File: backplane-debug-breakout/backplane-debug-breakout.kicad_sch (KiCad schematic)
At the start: 8 parts, among them J1 Conn_02x08_Odd_Even, J2 Conn_01x04, J3 Conn_01x01_Socket, J4 Conn_01x01_Socket, J5 Conn_01x04, SW1 SW_Push

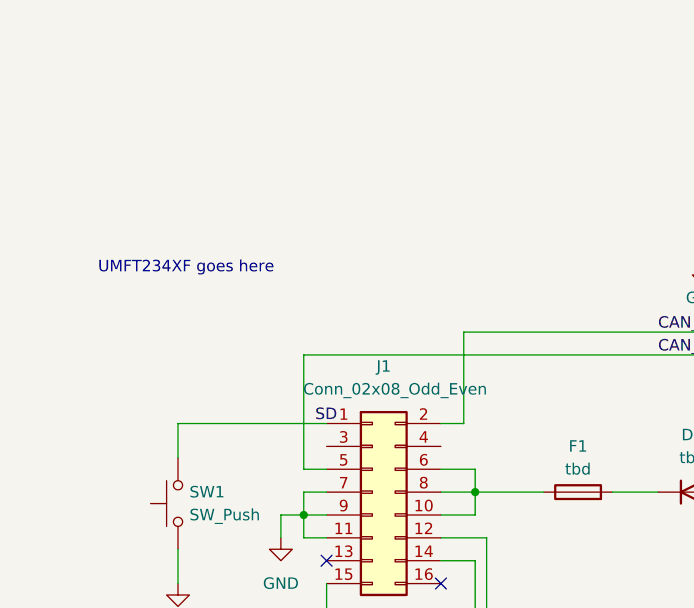
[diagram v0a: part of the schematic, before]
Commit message: added UMFT234XF to schematic
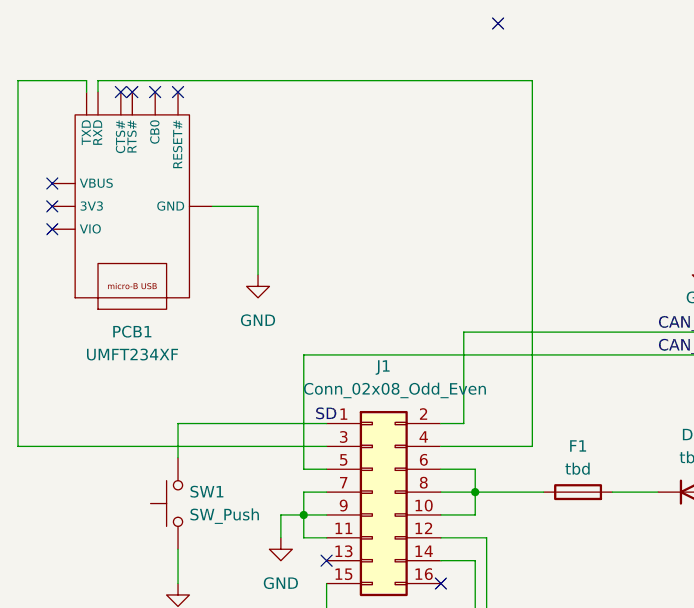
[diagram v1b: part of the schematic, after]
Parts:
- added PCB1: UMFT234XF, symbol oresat-pcbs:UMFT234XF
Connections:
- net GND: now also PCB1.P4 (GND)
- net at J1.3 (Pin_3): now also PCB1.P7 (TXD)
- net at J1.4 (Pin_4): now also PCB1.P9 (RXD)
- no-connect marks 3 -> 11
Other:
- note removed: "UMFT234XF goes here"
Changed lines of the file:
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@@
   (junction (at 120.65 80.01) (diameter 0) (color 0 0 0 0)
   )
+  (no_connect (at 123.19 27.94))
+  (no_connect (at 73.66 48.26))
   (no_connect (at 148.59 67.31))
+  (no_connect (at 81.28 35.56))
+  (no_connect (at 82.55 35.56))
+  (no_connect (at 73.66 50.8))
   (no_connect (at 104.14 87.63))
+  (no_connect (at 85.09 35.56))
+  (no_connect (at 73.66 45.72))
+  (no_connect (at 87.63 35.56))
   (no_connect (at 116.84 90.17))
   (wire (pts (xy 101.6 82.55) (xy 104.14 82.55))
@@
     (stroke (width 0) (type default))
   )
+  (wire (pts (xy 96.52 48.26) (xy 96.52 55.88))
+    (stroke (width 0) (type default))
+  )
   (wire (pts (xy 101.6 77.47) (xy 101.6 64.77))
     (stroke (width 0) (type default))
@@
     (stroke (width 0) (type default))
   )
+  (wire (pts (xy 69.85 74.93) (xy 104.14 74.93))
+    (stroke (width 0) (type default))
+  )
   (wire (pts (xy 148.59 59.69) (xy 148.59 53.34))
     (stroke (width 0) (type default))
   )
+  (wire (pts (xy 77.47 34.29) (xy 69.85 34.29))
+    (stroke (width 0) (type default))
+  )
   (wire (pts (xy 104.14 77.47) (xy 101.6 77.47))
     (stroke (width 0) (type default))
@@
     (stroke (width 0) (type default))
   )
+  (wire (pts (xy 127 34.29) (xy 127 74.93))
+    (stroke (width 0) (type default))
+  )
   (wire (pts (xy 104.14 80.01) (xy 101.6 80.01))
     (stroke (width 0) (type default))
@@
     (stroke (width 0) (type default))
   )
+  (wire (pts (xy 77.47 35.56) (xy 77.47 34.29))
+    (stroke (width 0) (type default))
+  )
   (wire (pts (xy 119.38 62.23) (xy 148.59 62.23))
     (stroke (width 0) (type default))
@@
     (stroke (width 0) (type default))
   )
+  (wire (pts (xy 78.74 34.29) (xy 127 34.29))
+    (stroke (width 0) (type default))
+  )
   (wire (pts (xy 148.59 80.01) (xy 154.94 80.01))
     (stroke (width 0) (type default))
@@
     (stroke (width 0) (type default))
   )
+  (wire (pts (xy 78.74 35.56) (xy 78.74 34.29))
+    (stroke (width 0) (type default))
+  )
+  (wire (pts (xy 69.85 34.29) (xy 69.85 74.93))
+    (stroke (width 0) (type default))
+  )
+  (wire (pts (xy 127 74.93) (xy 116.84 74.93))
+    (stroke (width 0) (type default))
+  )
   (wire (pts (xy 116.84 87.63) (xy 120.65 87.63))
     (stroke (width 0) (type default))
@@
     (stroke (width 0) (type default))
   )
+  (wire (pts (xy 91.44 48.26) (xy 96.52 48.26))
+    (stroke (width 0) (type default))
+  )
   (text "To vulCAN" (at 156.21 64.77 0)
     (effects (font (size 1.27 1.27)) (justify left bottom))
   )
-  (text "UMFT234XF goes here\n" (at 78.74 55.88 0)
-    (effects (font (size 1.27 1.27)) (justify left bottom))
-  )
   (text "OPD" (at 154.94 100.33 0)
     (effects (font (size 1.27 1.27)) (justify left bottom))
@@
     (pin "1")
     (instances
-      (project "flatsat-backplane-breakout-debug"
+      (project "backplane-debug-breakout"
         (path "/3c6f9748-3b52-445b-9cee-a3f7ec926272"
           (reference "D1") (unit 1)
@@
     )
   )
+  (symbol (lib_id "power:GND") (at 96.52 55.88 0) (unit 1)
+    (in_bom yes) (on_board yes) (dnp no) (fields_autoplaced)
+    (property "Reference" "#PWR06" (at 96.52 62.23 0)
+      (effects (font (size 1.27 1.27)) hide)
+    )
+    (property "Value" "GND" (at 96.52 60.96 0)
+      (effects (font (size 1.27 1.27)))
+    )
+    (property "Footprint" "" (at 96.52 55.88 0)
+      (effects (font (size 1.27 1.27)) hide)
+    )
+    (property "Datasheet" "" (at 96.52 55.88 0)
+      (effects (font (size 1.27 1.27)) hide)
+    )
+    (pin "1")
+    (instances
+      (project "backplane-debug-breakout"
+        (path "/3c6f9748-3b52-445b-9cee-a3f7ec926272"
+          (reference "#PWR06") (unit 1)
+        )
+      )
+    )
+  )
   (symbol (lib_id "Connector:Conn_01x01_Socket") (at 160.02 83.82 0) (unit 1)
     (in_bom yes) (on_board yes) (dnp no) (fields_autoplaced)
@@
     (pin "1")
     (instances
-      (project "flatsat-backplane-breakout-debug"
+      (project "backplane-debug-breakout"
         (path "/3c6f9748-3b52-445b-9cee-a3f7ec926272"
           (reference "J4") (unit 1)
@@
     (pin "1")
     (instances
-      (project "flatsat-backplane-breakout-debug"
+      (project "backplane-debug-breakout"
         (path "/3c6f9748-3b52-445b-9cee-a3f7ec926272"
           (reference "#PWR01") (unit 1)
@@
     (pin "2")
     (instances
-      (project "flatsat-backplane-breakout-debug"
+      (project "backplane-debug-breakout"
         (path "/3c6f9748-3b52-445b-9cee-a3f7ec926272"
           (reference "J1") (unit 1)
@@
     (pin "3")
     (instances
-      (project "flatsat-backplane-breakout-debug"
+      (project "backplane-debug-breakout"
         (path "/3c6f9748-3b52-445b-9cee-a3f7ec926272"
           (reference "J5") (unit 1)
@@
     (pin "2")
     (instances
-      (project "flatsat-backplane-breakout-debug"
+      (project "backplane-debug-breakout"
         (path "/3c6f9748-3b52-445b-9cee-a3f7ec926272"
           (reference "SW1") (unit 1)
@@
     (pin "4")
     (instances
-      (project "flatsat-backplane-breakout-debug"
+      (project "backplane-debug-breakout"
         (path "/3c6f9748-3b52-445b-9cee-a3f7ec926272"
           (reference "J2") (unit 1)
@@
     (pin "1")
     (instances
-      (project "flatsat-backplane-breakout-debug"
+      (project "backplane-debug-breakout"
         (path "/3c6f9748-3b52-445b-9cee-a3f7ec926272"
           (reference "#PWR05") (unit 1)
@@
     (pin "2")
     (instances
-      (project "flatsat-backplane-breakout-debug"
+      (project "backplane-debug-breakout"
         (path "/3c6f9748-3b52-445b-9cee-a3f7ec926272"
           (reference "F1") (unit 1)
@@
     (pin "1")
     (instances
-      (project "flatsat-backplane-breakout-debug"
+      (project "backplane-debug-breakout"
         (path "/3c6f9748-3b52-445b-9cee-a3f7ec926272"
           (reference "#PWR02") (unit 1)
@@
     (pin "1")
     (instances
-      (project "flatsat-backplane-breakout-debug"
+      (project "backplane-debug-breakout"
         (path "/3c6f9748-3b52-445b-9cee-a3f7ec926272"
           (reference "#PWR04") (unit 1)
@@
     (pin "1")
     (instances
-      (project "flatsat-backplane-breakout-debug"
+      (project "backplane-debug-breakout"
         (path "/3c6f9748-3b52-445b-9cee-a3f7ec926272"
           (reference "J3") (unit 1)
+        )
+      )
+    )
+  )
+  (symbol (lib_id "oresat-pcbs:UMFT234XF") (at 82.55 48.26 90) (unit 1)
+    (in_bom yes) (on_board yes) (dnp no) (fields_autoplaced)
+    (property "Reference" "PCB1" (at 82.55 62.23 90)
+      (effects (font (size 1.27 1.27)))
+    )
+    (property "Value" "UMFT234XF" (at 82.55 64.77 90)
+      (effects (font (size 1.27 1.27)))
+    )
+    (property "Footprint" "" (at 73.66 50.8 0)
+      (effects (font (size 1.27 1.27)) hide)
+    )
+    (property "Datasheet" "https://www.ftdichip.com/Support/Documents/DataSheets/Modules/DS_UMFT234XF.pdf" (at 57.15 48.26 0)
+      (effects (font (size 1.27 1.27)) hide)
+    )
+    (pin "P6")
+    (pin "P10")
+    (pin "P2")
+    (pin "P5")
+    (pin "P3")
+    (pin "P1")
+    (pin "P8")
+    (pin "P7")
+    (pin "P9")
+    (pin "P4")
+    (instances
+      (project "backplane-debug-breakout"
+        (path "/3c6f9748-3b52-445b-9cee-a3f7ec926272"
+          (reference "PCB1") (unit 1)
         )
       )
@@
     (pin "1")
     (instances
-      (project "flatsat-backplane-breakout-debug"
+      (project "backplane-debug-breakout"
         (path "/3c6f9748-3b52-445b-9cee-a3f7ec926272"
           (reference "#PWR03") (unit 1)

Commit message: rotated UMFT234XF and connected VIO to 3V3
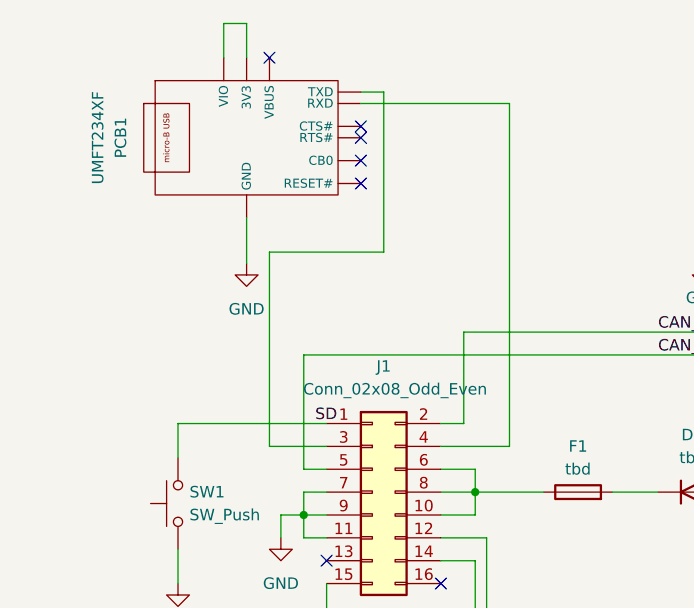
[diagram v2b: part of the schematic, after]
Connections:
- net at PCB1.P2 (3V3): now also PCB1.P3 (VIO)
- no-connect marks 11 -> 8
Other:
- moved on the sheet: PCB1
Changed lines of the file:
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@@
   (junction (at 120.65 80.01) (diameter 0) (color 0 0 0 0)
   )
-  (no_connect (at 123.19 27.94))
-  (no_connect (at 73.66 48.26))
   (no_connect (at 148.59 67.31))
-  (no_connect (at 81.28 35.56))
-  (no_connect (at 82.55 35.56))
-  (no_connect (at 73.66 50.8))
+  (no_connect (at 107.95 43.18))
+  (no_connect (at 107.95 40.64))
+  (no_connect (at 107.95 39.37))
+  (no_connect (at 107.95 45.72))
   (no_connect (at 104.14 87.63))
-  (no_connect (at 85.09 35.56))
-  (no_connect (at 73.66 45.72))
-  (no_connect (at 87.63 35.56))
+  (no_connect (at 97.79 31.75))
   (no_connect (at 116.84 90.17))
+  (wire (pts (xy 97.79 74.93) (xy 97.79 53.34))
+    (stroke (width 0) (type default))
+  )
   (wire (pts (xy 101.6 82.55) (xy 104.14 82.55))
     (stroke (width 0) (type default))
   )
+  (wire (pts (xy 110.49 53.34) (xy 110.49 35.56))
+    (stroke (width 0) (type default))
+  )
   (wire (pts (xy 101.6 64.77) (xy 148.59 64.77))
     (stroke (width 0) (type default))
@@
     (stroke (width 0) (type default))
   )
-  (wire (pts (xy 96.52 48.26) (xy 96.52 55.88))
-    (stroke (width 0) (type default))
-  )
   (wire (pts (xy 101.6 77.47) (xy 101.6 64.77))
     (stroke (width 0) (type default))
@@
     (stroke (width 0) (type default))
   )
+  (wire (pts (xy 97.79 53.34) (xy 110.49 53.34))
+    (stroke (width 0) (type default))
+  )
   (wire (pts (xy 121.92 85.09) (xy 121.92 95.25))
     (stroke (width 0) (type default))
@@
     (stroke (width 0) (type default))
   )
-  (wire (pts (xy 69.85 74.93) (xy 104.14 74.93))
+  (wire (pts (xy 95.25 27.94) (xy 95.25 31.75))
     (stroke (width 0) (type default))
   )
@@
     (stroke (width 0) (type default))
   )
-  (wire (pts (xy 77.47 34.29) (xy 69.85 34.29))
+  (wire (pts (xy 124.46 36.83) (xy 107.95 36.83))
     (stroke (width 0) (type default))
   )
@@
     (stroke (width 0) (type default))
   )
-  (wire (pts (xy 127 34.29) (xy 127 74.93))
+  (wire (pts (xy 92.71 27.94) (xy 92.71 31.75))
     (stroke (width 0) (type default))
   )
@@
     (stroke (width 0) (type default))
   )
-  (wire (pts (xy 77.47 35.56) (xy 77.47 34.29))
+  (wire (pts (xy 110.49 35.56) (xy 107.95 35.56))
     (stroke (width 0) (type default))
   )
@@
     (stroke (width 0) (type default))
   )
+  (wire (pts (xy 92.71 27.94) (xy 95.25 27.94))
+    (stroke (width 0) (type default))
+  )
   (wire (pts (xy 116.84 80.01) (xy 120.65 80.01))
     (stroke (width 0) (type default))
@@
     (stroke (width 0) (type default))
   )
+  (wire (pts (xy 124.46 74.93) (xy 124.46 36.83))
+    (stroke (width 0) (type default))
+  )
   (wire (pts (xy 87.63 86.36) (xy 87.63 90.17))
     (stroke (width 0) (type default))
@@
     (stroke (width 0) (type default))
   )
-  (wire (pts (xy 78.74 34.29) (xy 127 34.29))
-    (stroke (width 0) (type default))
-  )
   (wire (pts (xy 148.59 80.01) (xy 154.94 80.01))
     (stroke (width 0) (type default))
@@
     (stroke (width 0) (type default))
   )
-  (wire (pts (xy 78.74 35.56) (xy 78.74 34.29))
-    (stroke (width 0) (type default))
-  )
-  (wire (pts (xy 69.85 34.29) (xy 69.85 74.93))
-    (stroke (width 0) (type default))
-  )
-  (wire (pts (xy 127 74.93) (xy 116.84 74.93))
+  (wire (pts (xy 116.84 74.93) (xy 124.46 74.93))
+    (stroke (width 0) (type default))
+  )
+  (wire (pts (xy 104.14 74.93) (xy 97.79 74.93))
     (stroke (width 0) (type default))
   )
@@
     (stroke (width 0) (type default))
   )
-  (wire (pts (xy 91.44 48.26) (xy 96.52 48.26))
+  (wire (pts (xy 95.25 49.53) (xy 95.25 54.61))
     (stroke (width 0) (type default))
   )
@@
     )
   )
-  (symbol (lib_id "power:GND") (at 96.52 55.88 0) (unit 1)
-    (in_bom yes) (on_board yes) (dnp no) (fields_autoplaced)
-    (property "Reference" "#PWR06" (at 96.52 62.23 0)
-      (effects (font (size 1.27 1.27)) hide)
-    )
-    (property "Value" "GND" (at 96.52 60.96 0)
-      (effects (font (size 1.27 1.27)))
-    )
-    (property "Footprint" "" (at 96.52 55.88 0)
-      (effects (font (size 1.27 1.27)) hide)
-    )
-    (property "Datasheet" "" (at 96.52 55.88 0)
+  (symbol (lib_id "Connector:Conn_01x01_Socket") (at 160.02 83.82 0) (unit 1)
+    (in_bom yes) (on_board yes) (dnp no) (fields_autoplaced)
+    (property "Reference" "J4" (at 161.29 82.55 0)
+      (effects (font (size 1.27 1.27)) (justify left))
+    )
+    (property "Value" "Conn_01x01_Socket" (at 161.29 85.09 0)
+      (effects (font (size 1.27 1.27)) (justify left))
+    )
+    (property "Footprint" "" (at 160.02 83.82 0)
+      (effects (font (size 1.27 1.27)) hide)
+    )
+    (property "Datasheet" "~" (at 160.02 83.82 0)
+      (effects (font (size 1.27 1.27)) hide)
+    )
+    (pin "1")
+    (instances
+      (project "backplane-debug-breakout"
+        (path "/3c6f9748-3b52-445b-9cee-a3f7ec926272"
+          (reference "J4") (unit 1)
+        )
+      )
+    )
+  )
+  (symbol (lib_id "power:GND") (at 95.25 54.61 0) (unit 1)
+    (in_bom yes) (on_board yes) (dnp no) (fields_autoplaced)
+    (property "Reference" "#PWR06" (at 95.25 60.96 0)
+      (effects (font (size 1.27 1.27)) hide)
+    )
+    (property "Value" "GND" (at 95.25 59.69 0)
+      (effects (font (size 1.27 1.27)))
+    )
+    (property "Footprint" "" (at 95.25 54.61 0)
+      (effects (font (size 1.27 1.27)) hide)
+    )
+    (property "Datasheet" "" (at 95.25 54.61 0)
       (effects (font (size 1.27 1.27)) hide)
     )
@@
         (path "/3c6f9748-3b52-445b-9cee-a3f7ec926272"
           (reference "#PWR06") (unit 1)
-        )
-      )
-    )
-  )
-  (symbol (lib_id "Connector:Conn_01x01_Socket") (at 160.02 83.82 0) (unit 1)
-    (in_bom yes) (on_board yes) (dnp no) (fields_autoplaced)
-    (property "Reference" "J4" (at 161.29 82.55 0)
-      (effects (font (size 1.27 1.27)) (justify left))
-    )
-    (property "Value" "Conn_01x01_Socket" (at 161.29 85.09 0)
-      (effects (font (size 1.27 1.27)) (justify left))
-    )
-    (property "Footprint" "" (at 160.02 83.82 0)
-      (effects (font (size 1.27 1.27)) hide)
-    )
-    (property "Datasheet" "~" (at 160.02 83.82 0)
-      (effects (font (size 1.27 1.27)) hide)
-    )
-    (pin "1")
-    (instances
-      (project "backplane-debug-breakout"
-        (path "/3c6f9748-3b52-445b-9cee-a3f7ec926272"
-          (reference "J4") (unit 1)
         )
       )
@@
     )
   )
-  (symbol (lib_id "oresat-pcbs:UMFT234XF") (at 82.55 48.26 90) (unit 1)
-    (in_bom yes) (on_board yes) (dnp no) (fields_autoplaced)
-    (property "Reference" "PCB1" (at 82.55 62.23 90)
-      (effects (font (size 1.27 1.27)))
-    )
-    (property "Value" "UMFT234XF" (at 82.55 64.77 90)
-      (effects (font (size 1.27 1.27)))
-    )
-    (property "Footprint" "" (at 73.66 50.8 0)
-      (effects (font (size 1.27 1.27)) hide)
-    )
-    (property "Datasheet" "https://www.ftdichip.com/Support/Documents/DataSheets/Modules/DS_UMFT234XF.pdf" (at 57.15 48.26 0)
-      (effects (font (size 1.27 1.27)) hide)
-    )
+  (symbol (lib_id "oresat-pcbs:UMFT234XF") (at 95.25 40.64 0) (unit 1)
+    (in_bom yes) (on_board yes) (dnp no) (fields_autoplaced)
+    (property "Reference" "PCB1" (at 81.28 40.64 90)
+      (effects (font (size 1.27 1.27)))
+    )
+    (property "Value" "UMFT234XF" (at 78.74 40.64 90)
+      (effects (font (size 1.27 1.27)))
+    )
+    (property "Footprint" "" (at 92.71 31.75 0)
+      (effects (font (size 1.27 1.27)) hide)
+    )
+    (property "Datasheet" "https://www.ftdichip.com/Support/Documents/DataSheets/Modules/DS_UMFT234XF.pdf" (at 95.25 15.24 0)
+      (effects (font (size 1.27 1.27)) hide)
+    )
